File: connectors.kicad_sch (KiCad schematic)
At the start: 0 parts

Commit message: Redoing power stage and changing output stage accordingly
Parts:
- added JP?: Jumper_3_Open, symbol Jumper:Jumper_3_Open
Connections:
- new net +5V: JP?.3 (B)
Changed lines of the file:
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@@
 (kicad_sch (version 20211123) (generator eeschema)
   (paper "A4")
+  (wire (pts (xy 82.55 39.37) (xy 90.17 39.37))
+    (stroke (width 0) (type default) (color 0 0 0 0))
+  )
+  (symbol (lib_id "Jumper:Jumper_3_Open") (at 76.2 39.37 0) (unit 1)
+    (in_bom yes) (on_board yes) (fields_autoplaced)
+    (property "Reference" "JP?" (id 0) (at 76.2 33.02 0))
+    (property "Value" "Jumper_3_Open" (id 1) (at 76.2 35.56 0))
+    (property "Footprint" "" (id 2) (at 76.2 39.37 0)
+      (effects (font (size 1.27 1.27)) hide)
+    )
+    (property "Datasheet" "~" (id 3) (at 76.2 39.37 0)
+      (effects (font (size 1.27 1.27)) hide)
+    )
+    (pin "1")
+    (pin "2")
+    (pin "3")
+  )
+  (symbol (lib_id "power:+5V") (at 90.17 39.37 270) (unit 1)
+    (in_bom yes) (on_board yes) (fields_autoplaced)
+    (property "Reference" "#PWR?" (id 0) (at 86.36 39.37 0)
+      (effects (font (size 1.27 1.27)) hide)
+    )
+    (property "Value" "+5V" (id 1) (at 93.98 39.3699 90)
+      (effects (font (size 1.27 1.27)) (justify left))
+    )
+    (property "Footprint" "" (id 2) (at 90.17 39.37 0)
+      (effects (font (size 1.27 1.27)) hide)
+    )
+    (property "Datasheet" "" (id 3) (at 90.17 39.37 0)
+      (effects (font (size 1.27 1.27)) hide)
+    )
+    (pin "1")
+  )
 )

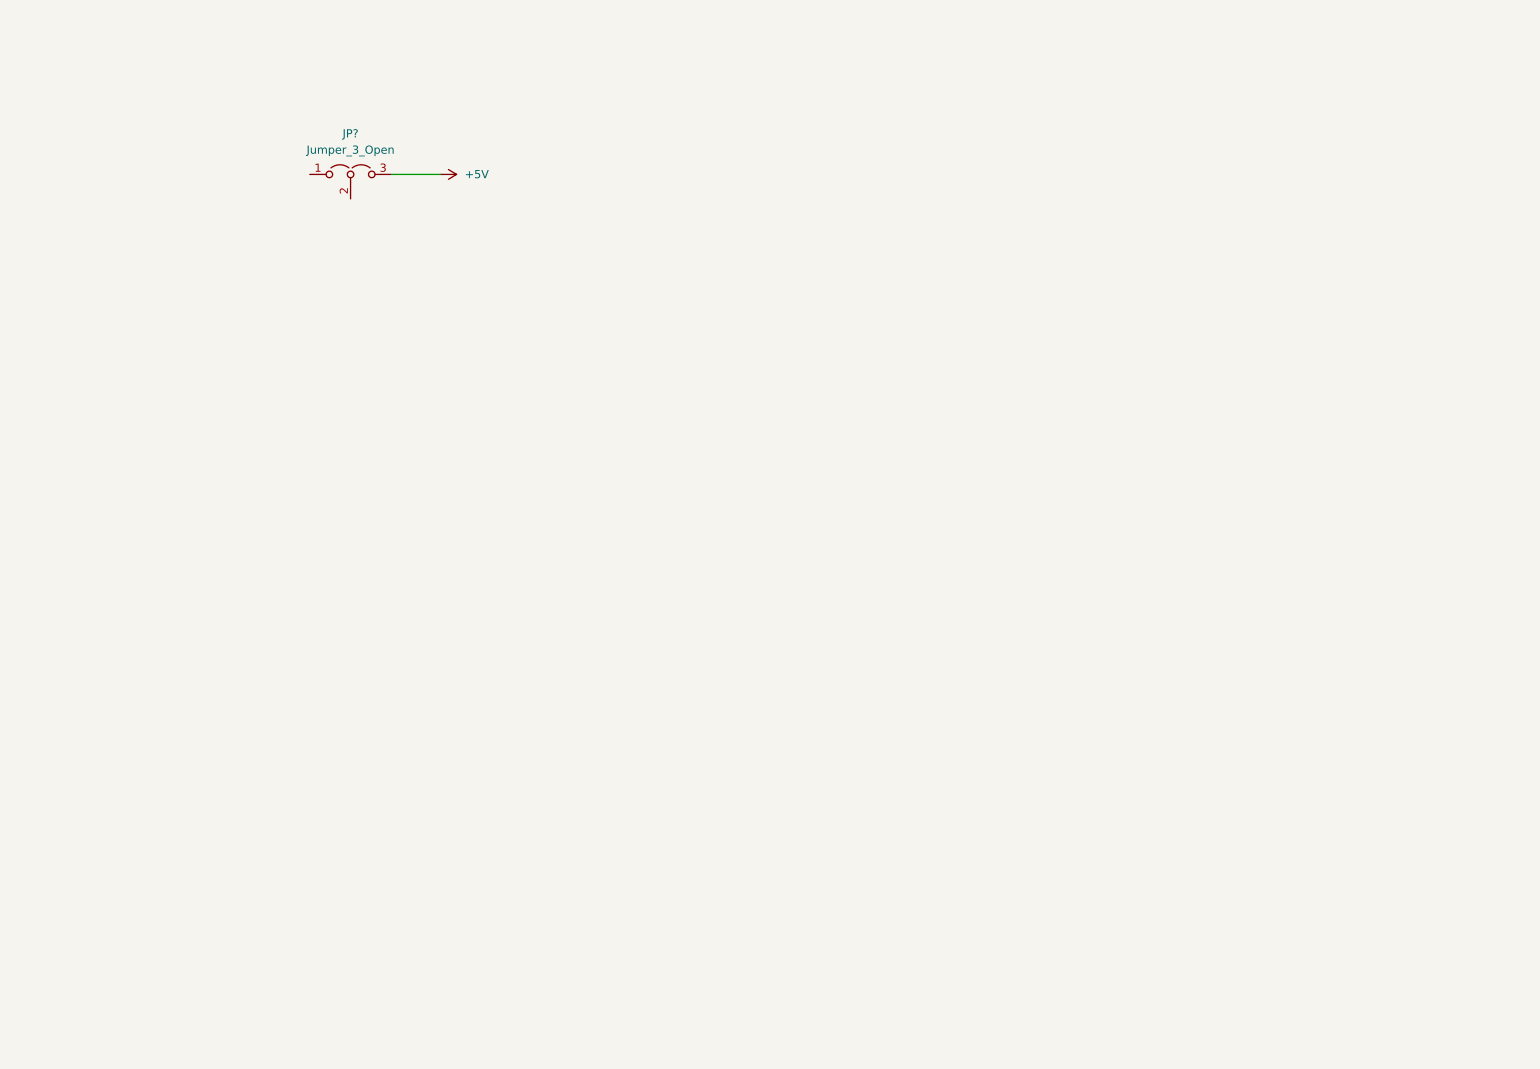
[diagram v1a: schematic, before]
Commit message: Finishing MCU interface. Adding connectors
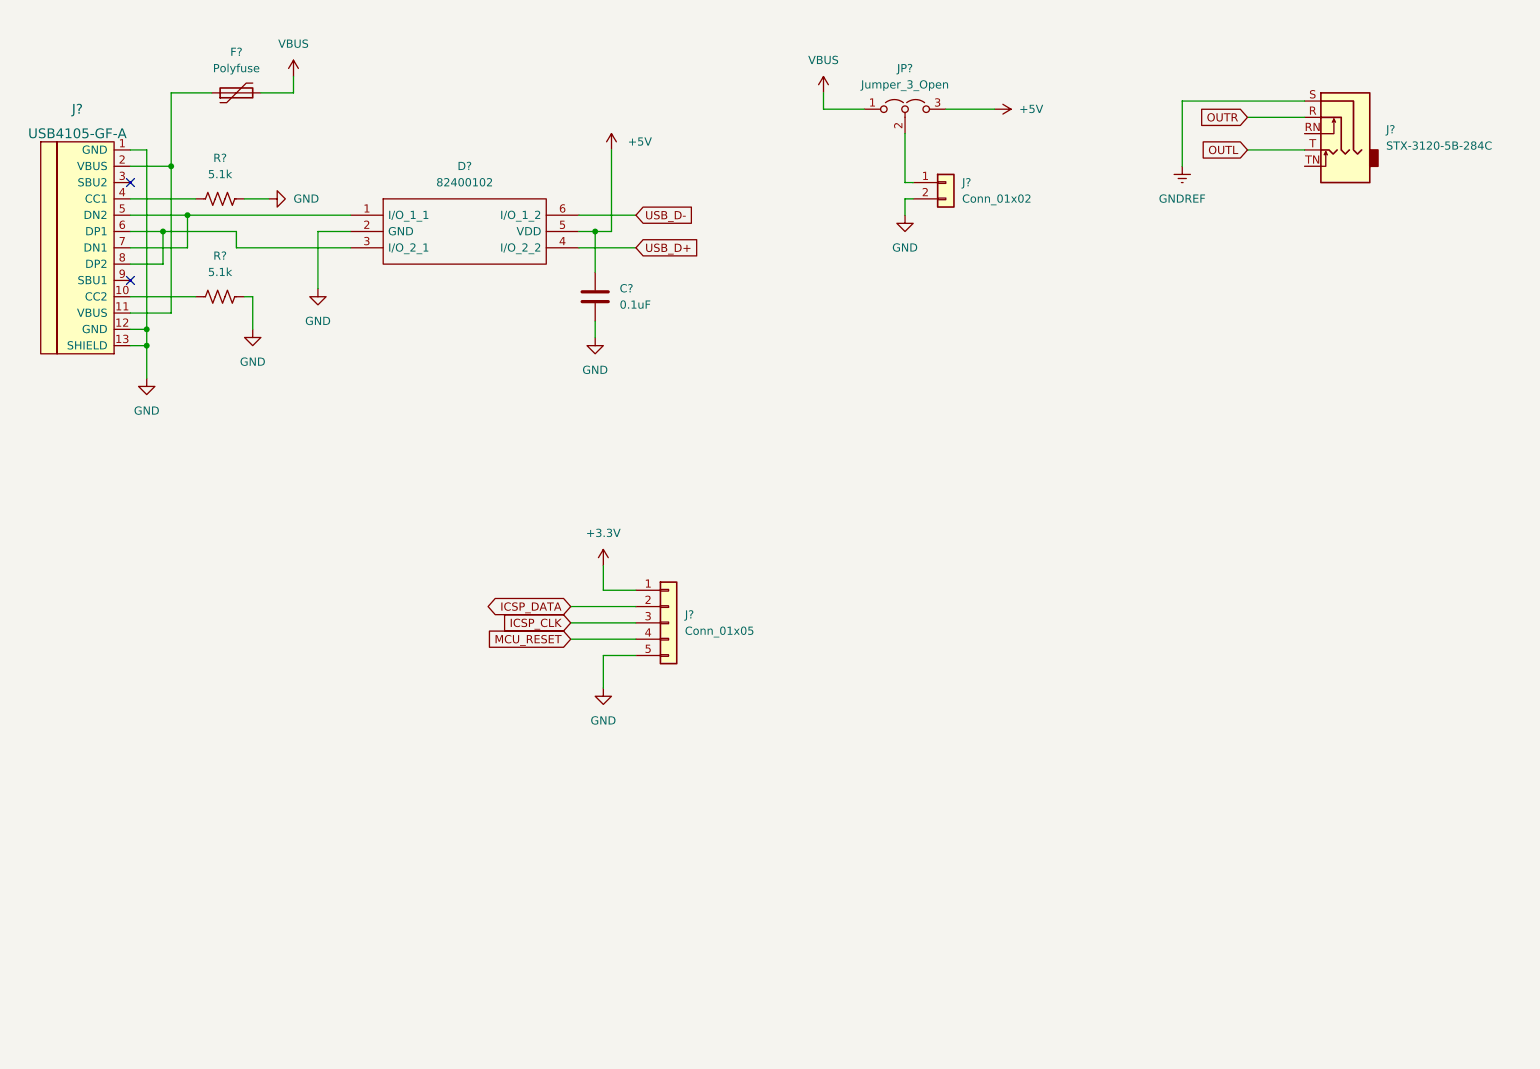
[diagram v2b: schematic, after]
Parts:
- added C?: 0.1uF, symbol Device:C
- added D?: 82400102, SOT95P280X145-6N, symbol SamacSys_Parts:82400102
- added F?: Polyfuse, symbol Device:Polyfuse
- added J?: Conn_01x05, symbol Connector_Generic:Conn_01x05
- added J?: USB4105-GF-A, symbol Type-C:HRO-TYPE-C-31-M-12
- added J?: Conn_01x02, symbol Connector_Generic:Conn_01x02
- added J?: STX-3120-5B-284C, symbol Connector:AudioJack3_SwitchTR
- added R? (x2): 5.1k, symbol Device:R_US
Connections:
- net +5V: now also C?.1, D?.5 (VDD)
- net VBUS: now reaches JP?.1 (A)
- net VBUS: now also F?.2
- net at JP?.2 (C): now also J?.1 (Pin_1)
- new net: J?.4 (CC1), R?.1
- new net: F?.1, J?.11 (VBUS), J?.2 (VBUS)
- new net: J?.10 (CC2), R?.1
- new net: D?.1 (I/O_1_1), J?.5 (DN2), J?.7 (DN1)
- new net: D?.3 (I/O_2_1), J?.6 (DP1), J?.8 (DP2)
- new net +3V3: J?.1 (Pin_1)
- new net GND: C?.2, D?.2 (GND), J?.1 (GND), J?.12 (GND), J?.13 (SHIELD), J?.2 (Pin_2), J?.5 (Pin_5), R?.2, R?.2
- new net GNDREF: J?.S
- new net ICSP_CLK: J?.3 (Pin_3)
- new net ICSP_DATA: J?.2 (Pin_2)
- new net MCU_RESET: J?.4 (Pin_4)
- new net OUTL: J?.T
- new net OUTR: J?.R
- new net USB_D+: D?.4 (I/O_2_2)
- new net USB_D-: D?.6 (I/O_1_2)
- no-connect marks 0 -> 2
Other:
- moved on the sheet: JP?

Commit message: Finishing Schematic. Fixed ERC errors
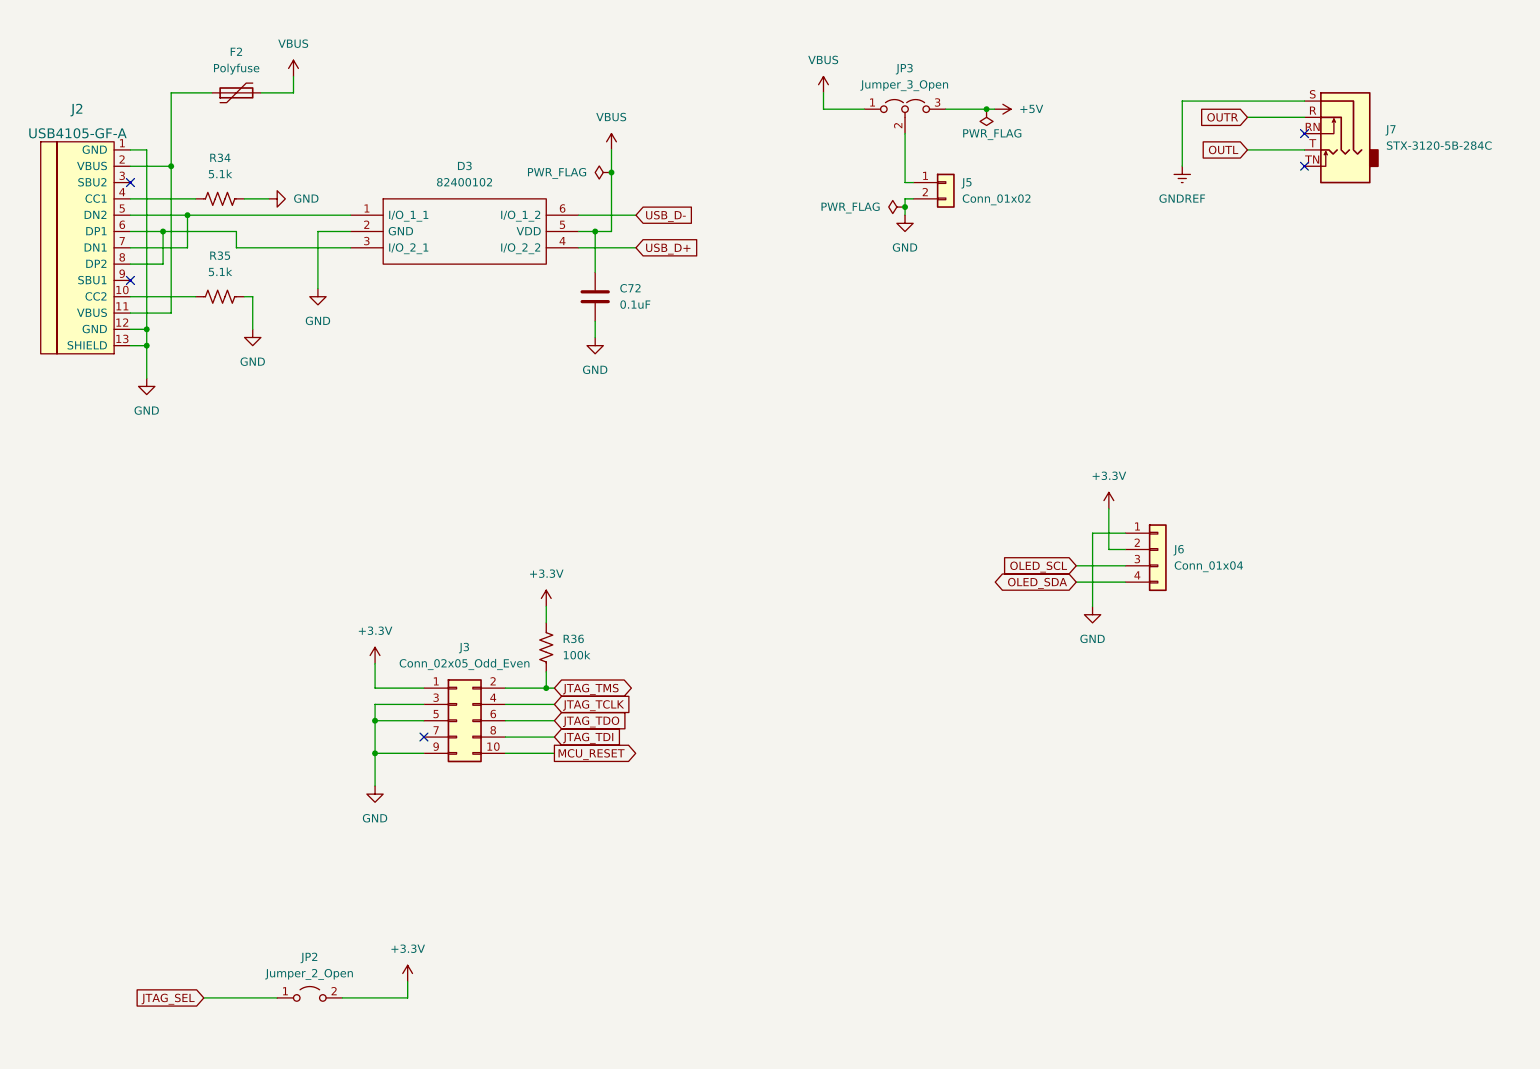
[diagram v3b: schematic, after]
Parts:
- removed J?: Conn_01x05, symbol Connector_Generic:Conn_01x05
- added J3: Conn_02x05_Odd_Even, symbol Connector_Generic:Conn_02x05_Odd_Even
- added J6: Conn_01x04, symbol Connector_Generic:Conn_01x04
- added JP2: Jumper_2_Open, symbol Jumper:Jumper_2_Open
- added R36: 100k, symbol Device:R_US
- gave numbers to parts that had none: 9
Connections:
- net +3V3: now also J3.1 (Pin_1), J6.2 (Pin_2), JP2.2 (B), R36.2
- net +5V: no longer C72.1, D3.5 (VDD)
- net GND: now also J3.3 (Pin_3), J3.5 (Pin_5), J3.9 (Pin_9), J6.1 (Pin_1)
- net MCU_RESET: now also J3.10 (Pin_10)
- net VBUS: now also C72.1, D3.5 (VDD)
- new net JTAG_SEL: JP2.1 (A)
- new net JTAG_TCLK: J3.4 (Pin_4)
- new net JTAG_TDI: J3.8 (Pin_8)
- new net JTAG_TDO: J3.6 (Pin_6)
- new net JTAG_TMS: J3.2 (Pin_2), R36.1
- new net OLED_SCL: J6.3 (Pin_3)
- new net OLED_SDA: J6.4 (Pin_4)
- no-connect marks 2 -> 5

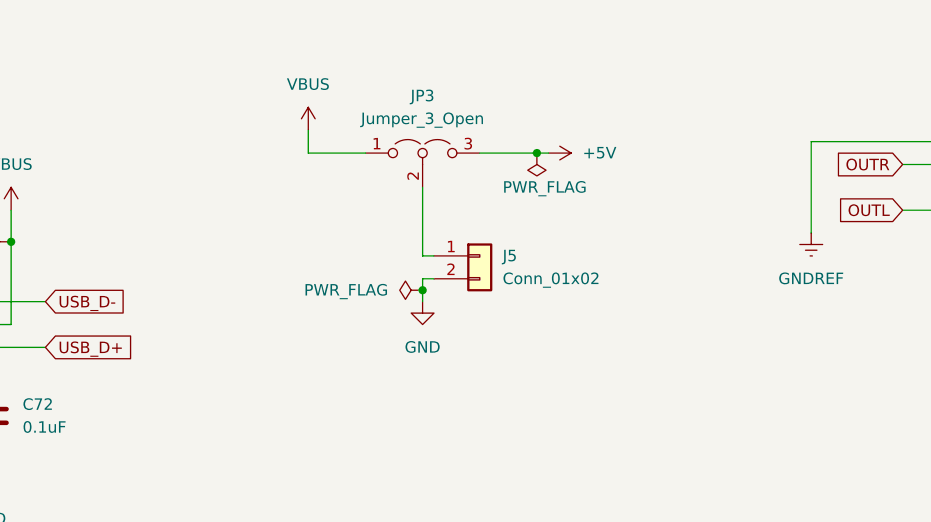
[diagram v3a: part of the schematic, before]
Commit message: Adding footprints
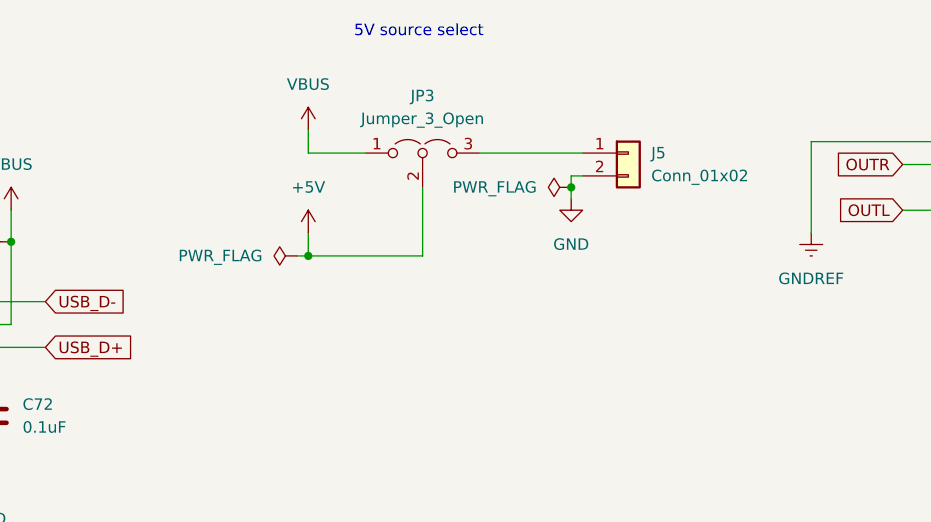
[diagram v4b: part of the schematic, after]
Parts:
- C72: footprint (none) -> Capacitor_SMD:C_0805_2012Metric_Pad1.18x1.45mm_HandSolder
- D3: footprint SOT95P280X145-6N -> SamacSys_Parts:SOT95P280X145-6N
- J5, JP2: footprint (none) -> Connector_PinHeader_2.54mm:PinHeader_1x02_P2.54mm_Vertical
- J6: footprint (none) -> Connector_PinHeader_2.54mm:PinHeader_1x04_P2.54mm_Vertical
- J7: footprint (none) -> SamacSys_Parts:STX31205B284C
- JP3: footprint (none) -> Connector_PinHeader_2.54mm:PinHeader_1x03_P2.54mm_Vertical
- R34, R35, R36: footprint (none) -> Resistor_SMD:R_0805_2012Metric_Pad1.20x1.40mm_HandSolder
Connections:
- net +5V: now also JP3.2 (C); no longer JP3.3 (B)
- net at J5.1 (Pin_1): now also JP3.3 (B); no longer JP3.2 (C)
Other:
- note added: "5V source select"
- moved on the sheet: J5
